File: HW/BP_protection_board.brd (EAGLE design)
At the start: 93.3 x 51.1 mm, 39 parts, among them IC1 74AC08D, K1 G5LE, K2 G5LE, Q1 2N7002, Q2 2N7002

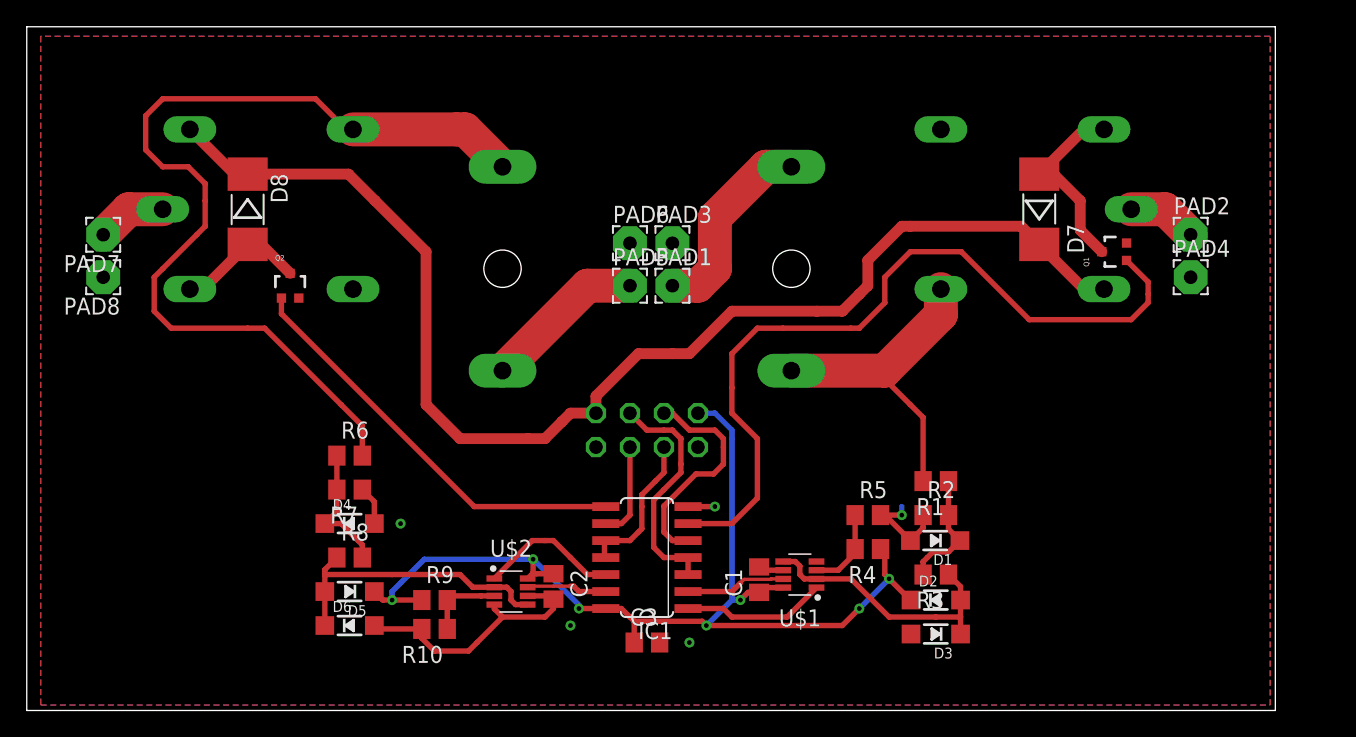
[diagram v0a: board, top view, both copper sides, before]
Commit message: Přidáno propojení desek fastony a distančními sloupky, změněna logika vyhodnocení nežádoucích stavů
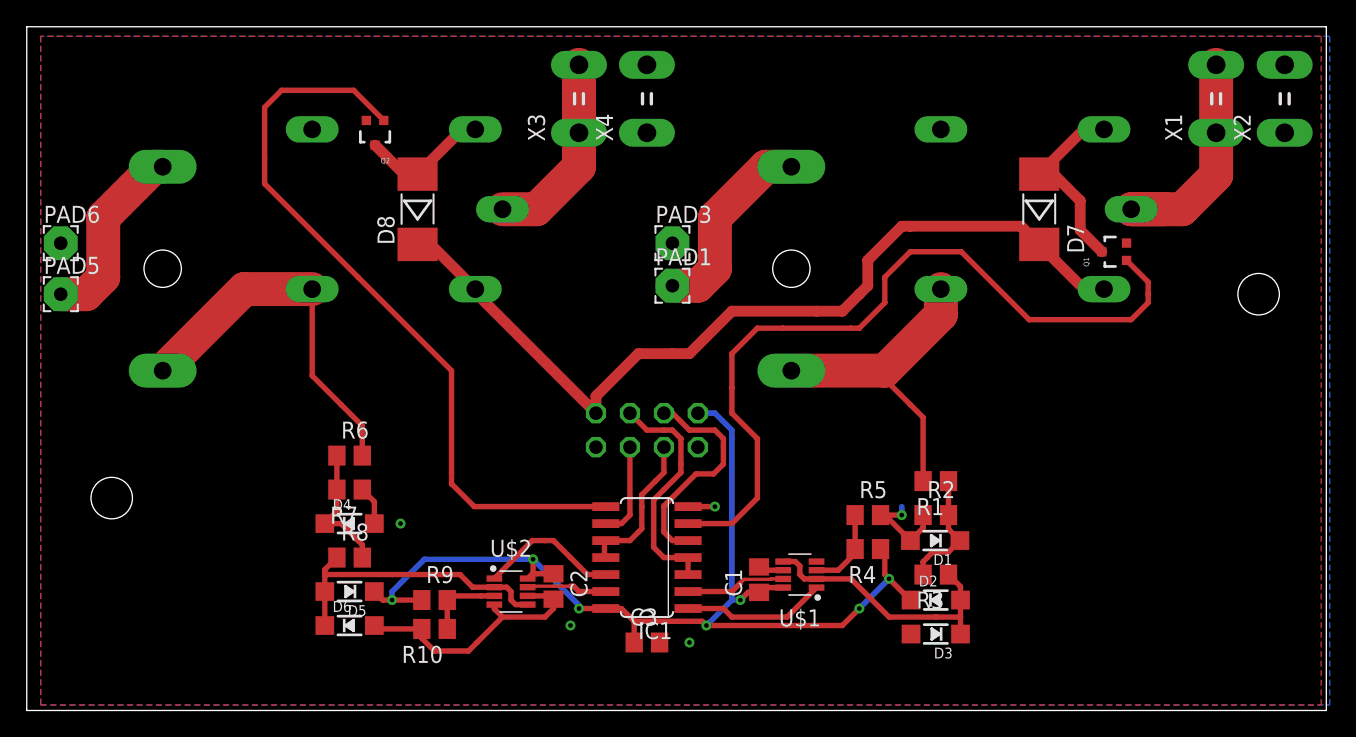
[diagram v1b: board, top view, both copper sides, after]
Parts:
- removed PAD2, PAD4, PAD7, PAD8: (no value), wirepad:2,54/1,0
- added X1, X2, X3, X4: (no value), con-rib:ST6,3
- moved PAD5 42.5 mm to (14.6, 61.6)
- moved PAD6 42.5 mm to (14.6, 65.4)
- moved F2 25.4 mm to (22.2, 63.5), turned to 270 degrees
- moved Q2 13.1 mm to (38.1, 73.7), turned to 180 degrees
- moved D8 12.7 mm to (41.3, 67.9), turned to 90 degrees
- moved K2 6.35 mm to (38.1, 67.9), turned to 0 degrees
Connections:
- net GND: now also X2.1, X2.2, X4.1, X4.2; no longer PAD4.1, PAD8.1
- net N$8: now also X1.1, X1.2; no longer PAD2.1
- net N$9: now also X3.1, X3.2; no longer PAD7.1
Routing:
- net OUT_FUSED: track 70.0 -> 27.7 mm
- net +5V: track 95.0 -> 66.3 mm
- net OUT_CONT: track 31.4 -> 56.5 mm
- net N$8: track 5.23 -> 18.2 mm
- net N$9: track 5.23 -> 14.7 mm
- net N$14: track 12.2 -> 14.2 mm
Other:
- board size 93.3 x 51.1 mm -> 97.1 x 51.1 mm

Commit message: Verze zadaná do výroby
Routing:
- net GND: track 34.2 -> 42.3 mm, vias 5 -> 10
- net N$8: track 18.2 -> 15.7 mm
- net IN_CONT: track 59.4 -> 60.9 mm
- net OUT_CONT: track 56.5 -> 57.3 mm
- removed copper zone on layer 1, net GND
